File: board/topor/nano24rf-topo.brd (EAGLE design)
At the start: 17.8 x 50 mm, 20 parts

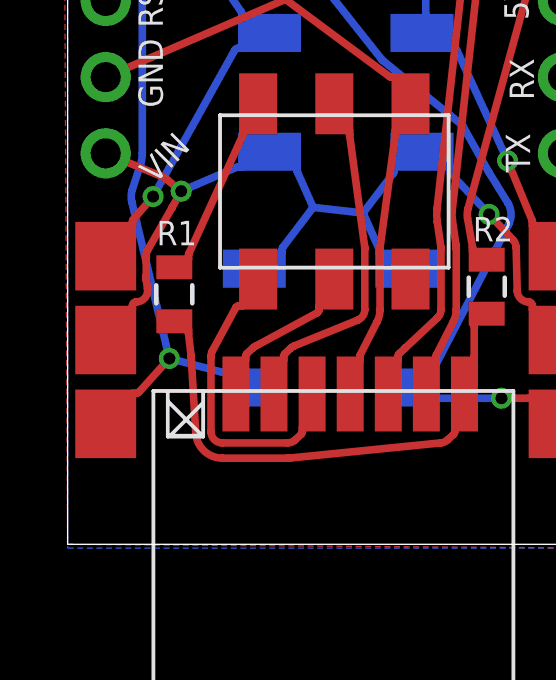
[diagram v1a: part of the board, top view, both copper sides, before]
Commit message: added FATPAD4
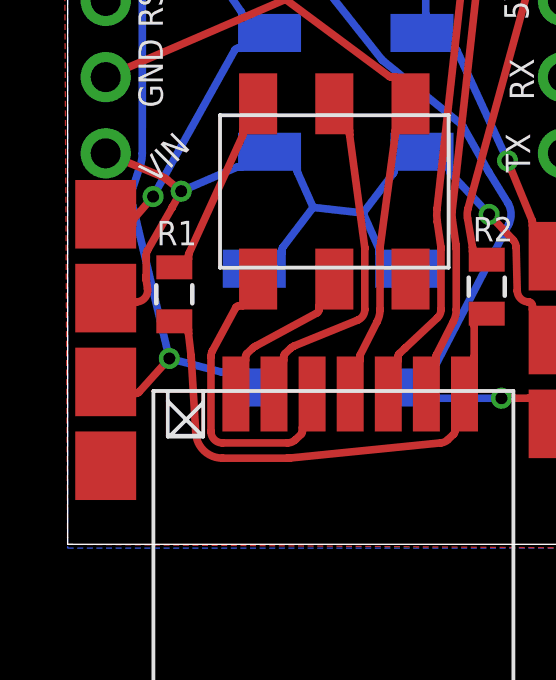
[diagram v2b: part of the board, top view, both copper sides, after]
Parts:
- U$6: device nanorf24:FATPAD -> nano24rf:FATPAD4
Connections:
- net FET03: no longer U$6.P$1
- net FET04: no longer U$6.P$3
- net VIN: no longer U$6.P$2
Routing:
- net VIN: track 32.7 -> 31.3 mm
- net FET04: track 31.3 -> 29.9 mm
- net FET03: track 39.2 -> 37.9 mm

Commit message: after topor
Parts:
- U$6: value 1X3SMD -> FATPAD4
- U$8: value 1X3SMD -> FATPAD4; device nanorf24:FATPAD -> nano24rf:FATPAD4
- moved Q3 5.18 mm to (6.22, 44.5), turned to 0 degrees
- moved R5 2.20 mm to (6.22, 40.8), turned to 180 degrees
- moved R1 0.68 mm to (3.81, 7.70)
- moved U$8 0.48 mm to (16.5, 6.35), turned to 270 degrees
- moved U$6 0.46 mm to (1.27, 6.35), turned to 270 degrees
- moved R2 0.40 mm to (14.1, 8.21)
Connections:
- net FET03: now also U$6.P$1
- net FET04: now also U$6.P$3
- net GND: now also U$6.P$4, U$8.P$4
- net VIN: now also U$6.P$2
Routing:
- net GND: track 91.1 -> 100.5 mm, vias 3 -> 0
- net FET03: track 37.9 -> 44.1 mm, vias 1 -> 2
- net MISO: track 10.3 -> 4.28 mm
- net FET02: track 16.5 -> 21.4 mm
- net MOSI: track 11.5 -> 15.5 mm
- net SCK: track 5.40 -> 9.01 mm
- net FET01: track 26.6 -> 23.1 mm
- net D9: track 12.1 -> 8.55 mm
- net FET04: track 29.9 -> 32.4 mm, vias 1 -> 3
- net D10: track 13.7 -> 11.7 mm
- net N$6: track 17.4 -> 16.2 mm, vias 0 -> 2
- net CE: track 31.5 -> 32.2 mm
- net 5V: track 6.25 -> 6.76 mm
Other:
- board text added: "M1"
- board text added: "V+"
